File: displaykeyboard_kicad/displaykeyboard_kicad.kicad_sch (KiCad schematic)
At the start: 1 part, among them U1 Sparkfun_Pro_Micro

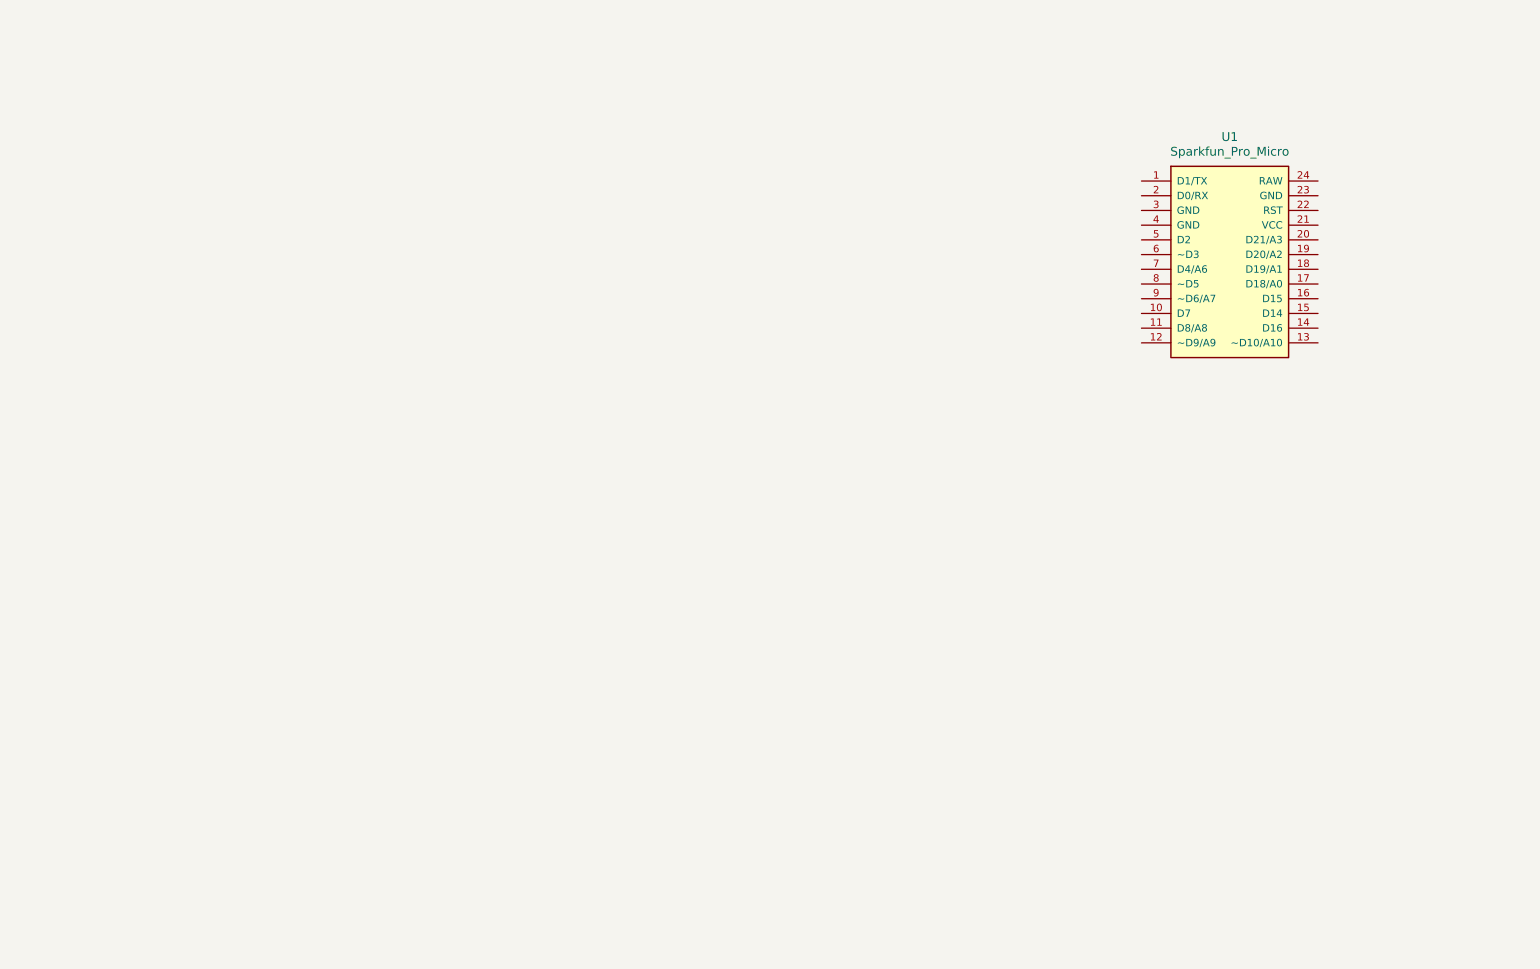
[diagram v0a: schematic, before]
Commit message: Add footprints & update KiCad project files
Add backup archives and new SuperNano footprints/symbols, and update KiCad project and schematic files.

- Added three backup ZIPs under displaykeyboard_kicad/displaykeyboard_kicad-backups.
- Added footprint files for SuperNano (ESP32-S3-SuperMini.kicad_mod, superMini Nrf52840.kicad_mod, superMini.kicad_sym) and a .bak file under footprint/supernano.
- Updated displaykeyboard_kicad.kicad_prl: expanded net inspector column defaults and set sorting_column to 0.
- Updated displaykeyboard_kicad.kicad_pro: large addition of board design_settings (DRC/rules, teardrop/tuning, via/track settings), added additional pcbnew last_paths entries, spice and project preferences, and updated used_designators.
- Updated displaykeyboard_kicad.kicad_sch: replaced/added symbol definitions (MCP73871 battery charger, OLED, SW_PUSH, TCA9548A I2C switch, supermini NRF52840, etc.), adjusted pin types/numbers/positions and formatting across many symbols.

These changes add footprints and update project/default settings and schematic symbols to match the new hardware and layout preferences.
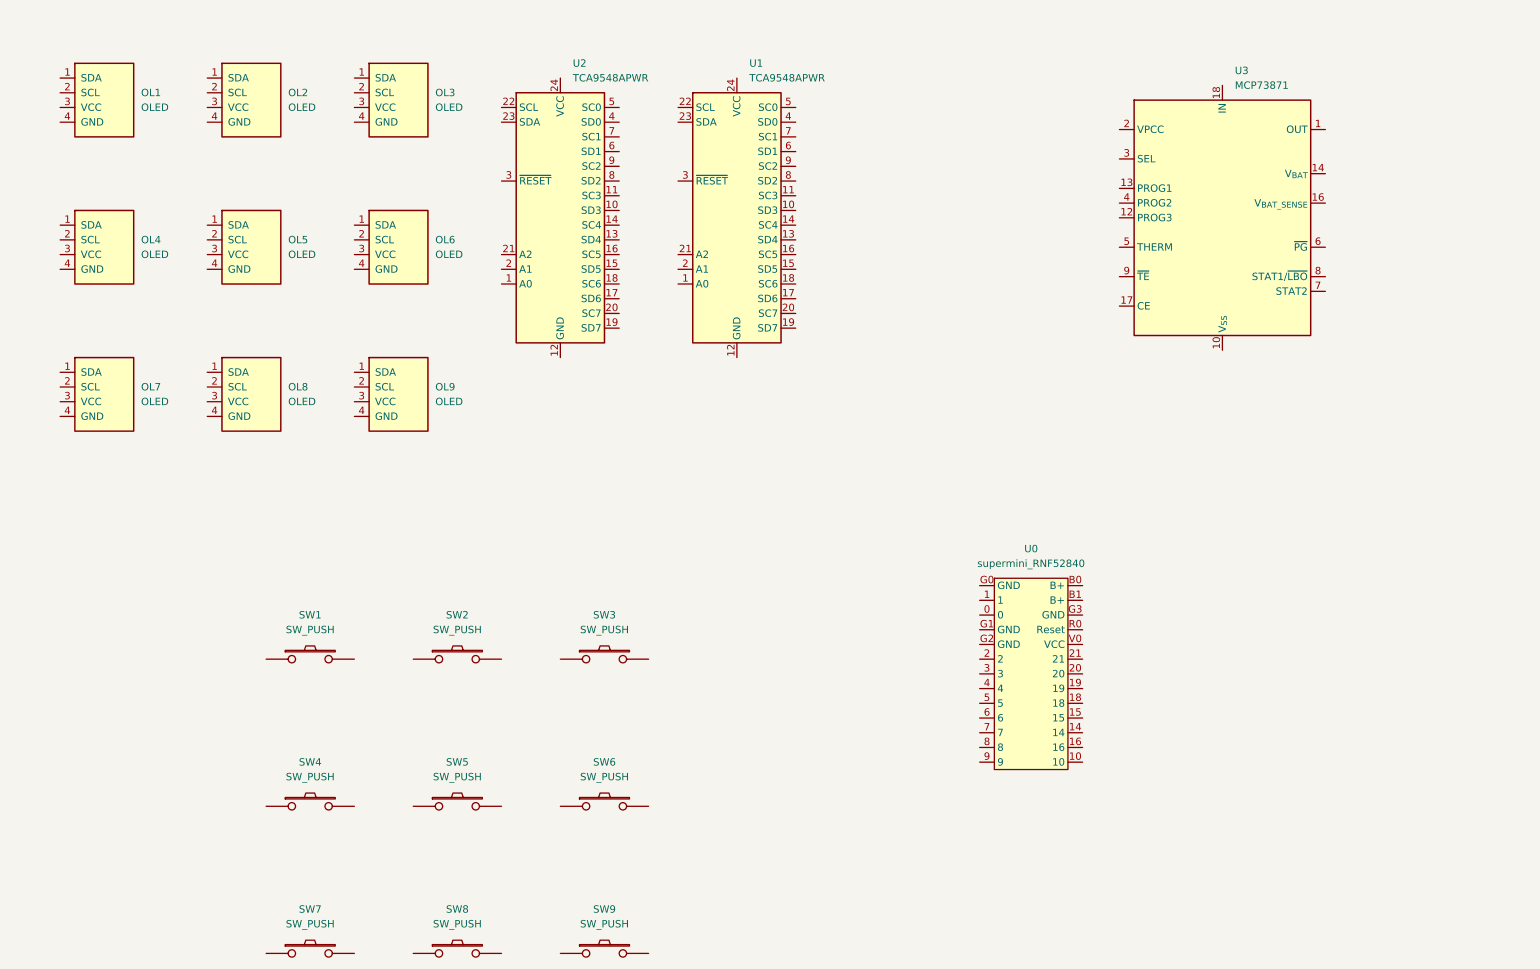
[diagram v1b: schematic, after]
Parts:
- removed U1: Sparkfun_Pro_Micro, Arduino:Sparkfun_Pro_Micro, symbol Arduino:Sparkfun_Pro_Micro
- added OL1, OL2, OL3, OL4, OL5, OL6, OL7, OL8, OL9: OLED, symbol BrownSugar_KBD:OLED
- added SW1, SW2, SW3, SW4, SW5, SW6, SW7, SW8, SW9: SW_PUSH, symbol BrownSugar_KBD:SW_PUSH
- added U0: supermini_RNF52840, symbol superMini:supermini_NRF52840
- added U1, U2: TCA9548APWR, Package_SO:TSSOP-24_4.4x7.8mm_P0.65mm, symbol Interface_Expansion:TCA9548APWR
- added U3: MCP73871, Package_DFN_QFN:QFN-20-1EP_4x4mm_P0.5mm_EP2.5x2.5mm, symbol Battery_Management:MCP73871
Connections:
- new net: U3.1 (OUT), U3.20 (OUT)
- new net: U3.10 (V_{SS}), U3.11 (V_{SS}), U3.21 (V_{SS})
- new net: U3.14 (V_{BAT}), U3.15 (V_{BAT})
- new net: U3.18 (IN), U3.19 (IN)

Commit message: main
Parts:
- removed OL9: OLED, symbol BrownSugar_KBD:OLED
- removed SW9: SW_PUSH, symbol BrownSugar_KBD:SW_PUSH
- removed U0: supermini_RNF52840, symbol superMini:supermini_NRF52840
- removed U2: TCA9548APWR, Package_SO:TSSOP-24_4.4x7.8mm_P0.65mm, symbol Interface_Expansion:TCA9548APWR
- removed U3: MCP73871, Package_DFN_QFN:QFN-20-1EP_4x4mm_P0.5mm_EP2.5x2.5mm, symbol Battery_Management:MCP73871
- added BT1: Battery_Cell, symbol Device:Battery_Cell
- added D1, D2, D3, D4, D5, D6, D7, D8: 1N4148W, Diode_SMD:D_SOD-123, symbol Diode:1N4148W
- added U4: XIAO-nRF52840-DIP, Seeed_Studio_XIAO_Series:XIAO-nRF52840-DIP, symbol Seeed_Studio_XIAO_Series:XIAO-nRF52840-DIP
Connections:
- net at OL6.1 (SDA): now also U1.15 (SD5)
- net at OL6.2 (SCL): now also U1.16 (SC5)
- net at OL6.3 (VCC): now also OL1.3 (VCC), OL2.3 (VCC), OL3.3 (VCC), OL4.3 (VCC), OL5.3 (VCC), OL7.3 (VCC), OL8.3 (VCC)
- net GND: now reaches OL6.4 (GND)
- net GND: now also OL1.4 (GND), OL2.4 (GND), OL3.4 (GND), OL4.4 (GND), OL5.4 (GND), OL7.4 (GND), OL8.4 (GND), U1.12 (GND), U4.13 (GND)
- net at OL7.1 (SDA): now also U1.17 (SD6)
- net at OL7.2 (SCL): now also U1.18 (SC6)
- net at OL3.1 (SDA): now also U1.8 (SD2)
- net at OL3.2 (SCL): now also U1.9 (SC2)
- net 1: now reaches SW1.1
- net 1: now also SW3.1, SW6.1, U4.2 (P0.03_A1_D1)
- net at SW1.2: now also D1.2 (A)
- net at OL5.1 (SDA): now also U1.13 (SD4)
- net at OL5.2 (SCL): now also U1.14 (SC4)
- net at SW6.2: now also D6.2 (A)
- net at SW3.2: now also D3.2 (A)
- net 3: now reaches SW8.1
- net 3: now also SW5.1, U4.4 (P0.29_A3_D3)
- net at SW8.2: now also D8.2 (A)
- net 2: now reaches SW4.1
- net 2: now also SW2.1, SW7.1, U4.3 (P0.28_A2_D2)
- net at SW4.2: now also D4.2 (A)
- net at OL2.1 (SDA): now also U1.6 (SD1)
- net at OL2.2 (SCL): now also U1.7 (SC1)
- net at SW5.2: now also D5.2 (A)
- net at SW2.2: now also D2.2 (A)
- net at OL1.1 (SDA): now also U1.4 (SD0)
- net at OL1.2 (SCL): now also U1.5 (SC0)
- net at SW7.2: now also D7.2 (A)
- net at U1.10 (SD3): now also OL4.1 (SDA)
- net at U1.11 (SC3): now also OL4.2 (SCL)
- net at U1.19 (SD7): now also OL8.1 (SDA)
- net at U1.20 (SC7): now also OL8.2 (SCL)
- net 8: now reaches U1.22 (SCL)
- net 8: now also U4.6 (P0.05_A5_D5_SCL)
- net 7: now reaches U1.23 (SDA)
- net 7: now also U4.5 (P0.04_A4_D4_SDA)
- new net 4: D1.1 (K), D2.1 (K), U4.8 (P1.12_D7_RX)
- new net 5: D3.1 (K), D4.1 (K), D5.1 (K), U4.9 (P1.13_D8_SCK)
- new net 6: D6.1 (K), D7.1 (K), D8.1 (K), U4.10 (P1.14_D9_MISO)
- new net B+: BT1.1 (+), U4.15 (BAT+)
- new net B-: BT1.2 (-), U4.16 (BAT-)
- no-connect marks 0 -> 8
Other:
- moved on the sheet: OL1, OL2, OL3, OL4, OL5, OL6, SW1, SW2, U1

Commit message: main
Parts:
- added SW9: SW_DIP_x01, symbol Switch:SW_DIP_x01
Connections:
- net GND: now also SW9.2
- net 9: now reaches U4.7 (P1.11_D6_TX)
- net 9: now also SW9.1
- no-connect marks 8 -> 7
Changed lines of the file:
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@@
 	)
 	(no_connect
-		(at 133.35 118.11)
-	)
-	(no_connect
 		(at 129.54 95.25)
 	)
@@
 	(wire
 		(pts
+			(xy 111.76 147.32) (xy 111.76 151.13)
+		)
+		(stroke
+			(width 0)
+			(type default)
+		)
+	)
+	(wire
+		(pts
 			(xy 248.92 31.75) (xy 248.92 35.56)
 		)
@@
 	(wire
 		(pts
+			(xy 107.95 147.32) (xy 111.76 147.32)
+		)
+		(stroke
+			(width 0)
+			(type default)
+		)
+	)
+	(wire
+		(pts
 			(xy 255.27 54.61) (xy 255.27 68.58)
 		)
@@
 	(wire
 		(pts
+			(xy 129.54 118.11) (xy 133.35 118.11)
+		)
+		(stroke
+			(width 0)
+			(type default)
+		)
+	)
+	(wire
+		(pts
 			(xy 255.27 54.61) (xy 261.62 54.61)
 		)
@@
 	(wire
 		(pts
+			(xy 90.17 147.32) (xy 92.71 147.32)
+		)
+		(stroke
+			(width 0)
+			(type default)
+		)
+	)
+	(wire
+		(pts
 			(xy 186.69 99.06) (xy 186.69 101.6)
 		)
@@
 		)
 	)
+	(global_label "9"
+		(shape input)
+		(at 90.17 147.32 180)
+		(fields_autoplaced yes)
+		(effects
+			(font
+				(size 1.27 1.27)
+			)
+			(justify right)
+		)
+		(property "Intersheetrefs" "${INTERSHEET_REFS}"
+			(at 85.9753 147.32 0)
+			(hide yes)
+			(show_name no)
+			(do_not_autoplace no)
+			(effects
+				(font
+					(size 1.27 1.27)
+				)
+				(justify right)
+			)
+		)
+	)
 	(global_label "5"
 		(shape input)
@@
 		)
 	)
+	(global_label "9"
+		(shape input)
+		(at 129.54 118.11 180)
+		(fields_autoplaced yes)
+		(effects
+			(font
+				(size 1.27 1.27)
+			)
+			(justify right)
+		)
+		(property "Intersheetrefs" "${INTERSHEET_REFS}"
+			(at 125.3453 118.11 0)
+			(hide yes)
+			(show_name no)
+			(do_not_autoplace no)
+			(effects
+				(font
+					(size 1.27 1.27)
+				)
+				(justify right)
+			)
+		)
+	)
 	(global_label "B+"
 		(shape input)
@@
 	)
 	(symbol
+		(lib_id "Switch:SW_DIP_x01")
+		(at 100.33 147.32 0)
+		(unit 1)
+		(body_style 1)
+		(exclude_from_sim no)
+		(in_bom yes)
+		(on_board yes)
+		(in_pos_files yes)
+		(dnp no)
+		(fields_autoplaced yes)
+		(property "Reference" "SW9"
+			(at 100.33 139.7 0)
+			(show_name no)
+			(do_not_autoplace no)
+			(effects
+				(font
+					(size 1.27 1.27)
+				)
+			)
+		)
+		(property "Value" "SW_DIP_x01"
+			(at 100.33 142.24 0)
+			(show_name no)
+			(do_not_autoplace no)
+			(effects
+				(font
+					(size 1.27 1.27)
+				)
+			)
+		)
+		(property "Footprint" ""
+			(at 100.33 147.32 0)
+			(hide yes)
+			(show_name no)
+			(do_not_autoplace no)
+			(effects
+				(font
+					(size 1.27 1.27)
+				)
+			)
+		)
+		(property "Datasheet" ""
+			(at 100.33 147.32 0)
+			(hide yes)
+			(show_name no)
+			(do_not_autoplace no)
+			(effects
+				(font
+					(size 1.27 1.27)
+				)
+			)
+		)
+		(property "Description" "1x DIP Switch, Single Pole Single Throw (SPST) switch, small symbol"
+			(at 100.33 147.32 0)
+			(hide yes)
+			(show_name no)
+			(do_not_autoplace no)
+			(effects
+				(font
+					(size 1.27 1.27)
+				)
+			)
+		)
+		(pin "1"
+		)
+		(pin "2"
+		)
+		(instances
+			(project "displaykeyboard_kicad"
+				(path "/fccedd88-d7cb-4cc9-8b23-c573142a04a1"
+					(reference "SW9")
+					(unit 1)
+				)
+			)
+		)
+	)
+	(symbol
 		(lib_id "BrownSugar_KBD:OLED")
 		(at 269.24 53.34 0)
@@
 					(unit 1)
 				)
+			)
+		)
+	)
+	(symbol
+		(lib_id "power:GND")
+		(at 111.76 151.13 0)
+		(unit 1)
+		(body_style 1)
+		(exclude_from_sim no)
+		(in_bom yes)
+		(on_board yes)
+		(in_pos_files yes)
+		(dnp no)
+		(fields_autoplaced yes)
+		(property "Reference" "#PWR04"
+			(at 111.76 157.48 0)
+			(hide yes)
+			(show_name no)
+			(do_not_autoplace no)
+			(effects
+				(font
+					(size 1.27 1.27)
+				)
+			)
+		)
+		(property "Value" "GND"
+			(at 111.76 156.21 0)
+			(show_name no)
+			(do_not_autoplace no)
+			(effects
+				(font
+					(size 1.27 1.27)
+				)
+			)
+		)
+		(property "Footprint" ""
+			(at 111.76 151.13 0)
+			(hide yes)
+			(show_name no)
+			(do_not_autoplace no)
+			(effects
+				(font
+					(size 1.27 1.27)
+				)
+			)
+		)
+		(property "Datasheet" ""
+			(at 111.76 151.13 0)
+			(hide yes)
+			(show_name no)
+			(do_not_autoplace no)
+			(effects
+				(font
+					(size 1.27 1.27)
+				)
+			)
+		)
+		(property "Description" "Power symbol creates a global label with name \"GND\" , ground"
+			(at 111.76 151.13 0)
+			(hide yes)
+			(show_name no)
+			(do_not_autoplace no)
+			(effects
+				(font
+					(size 1.27 1.27)
+				)
+			)
+		)
+		(pin "1"
+		)
+		(instances
+			(project "displaykeyboard_kicad"
+				(path "/fccedd88-d7cb-4cc9-8b23-c573142a04a1"
+					(reference "#PWR04")
+					(unit 1)
+				)
